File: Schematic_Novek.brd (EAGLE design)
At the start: 160 x 100 mm, 42 parts, among them IC1 STM32F10XCXT6, J2 1X2-3.5MM, J3 1X2-3.5MM, Q1 2N2907, U1 BQ21040, U2 MAX17048G+T10, U3 HX711

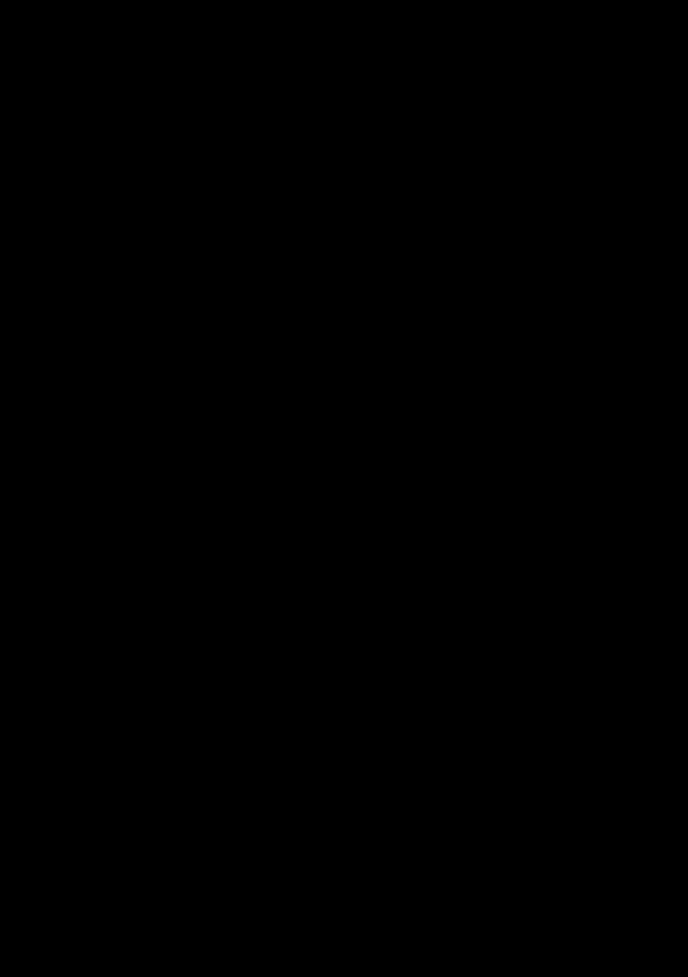
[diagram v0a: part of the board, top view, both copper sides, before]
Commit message: Adds sensor ports
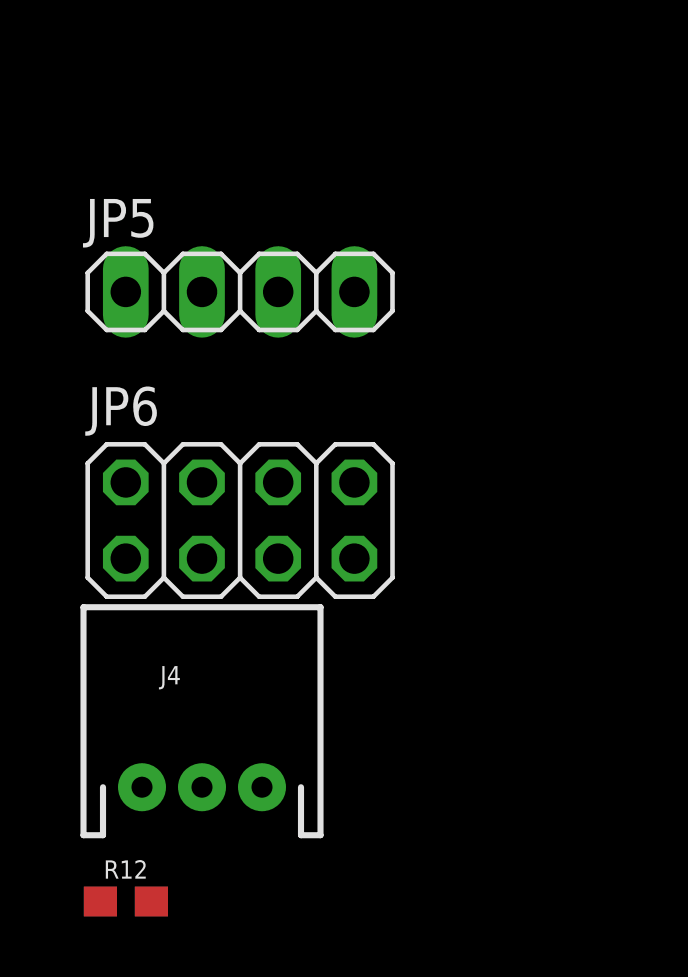
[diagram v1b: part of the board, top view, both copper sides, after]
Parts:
- added J4: (no value), SparkFun-Connectors:JST-3-PTH
- added JP5: (no value), pinhead:1X04
- added JP6: (no value), pinhead:2X04
- added R12: 10k, SparkFun-Resistors:0603
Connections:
- new net DATA_DHT: IC1.17, J4.2
- new net ESP8266_RX: IC1.12, JP6.2
- new net ESP8266_TX: IC1.13, JP6.7
- net 3.3V: now also C15.2, J4.1, JP5.3, JP6.1, Q1.E, R12.1, U3.1, U3.16
- net DOUT_HX: now also IC1.14
- net GND: now also J4.3, JP5.4, JP6.8
- net N$6: now also JP6.5, R12.2; no longer C15.2, Q1.E, U3.1, U3.16
- net SCK_HX: now also IC1.15
- net SCL: now also JP5.1
- net SDA: now also JP5.2
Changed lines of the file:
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@@
 <attribute name="NAME" x="-46.53" y="-203.28" size="1.27" layer="25" rot="R180"/>
+</element>
+<element name="JP5" library="pinhead" library_urn="urn:adsk.eagle:library:325" package="1X04" package3d_urn="urn:adsk.eagle:package:22407/2" value="" x="-46.99" y="-223.52" smashed="yes">
+<attribute name="NAME" x="-52.1462" y="-221.6912" size="1.27" layer="25" ratio="10"/>
+<attribute name="POPULARITY" value="91" x="-46.99" y="-223.52" size="1.778" layer="27" display="off"/>
+<attribute name="VALUE" x="-52.07" y="-226.695" size="1.27" layer="27"/>
+</element>
+<element name="JP6" library="pinhead" library_urn="urn:adsk.eagle:library:325" package="2X04" package3d_urn="urn:adsk.eagle:package:22461/2" value="" x="-46.99" y="-231.14" smashed="yes">
+<attribute name="NAME" x="-52.07" y="-227.965" size="1.27" layer="25" ratio="10"/>
+<attribute name="POPULARITY" value="47" x="-46.99" y="-231.14" size="1.778" layer="27" display="off"/>
+<attribute name="VALUE" x="-52.07" y="-235.585" size="1.27" layer="27"/>
+</element>
+<element name="J4" library="SparkFun-Connectors" package="JST-3-PTH" value="" x="-48.26" y="-240.03" smashed="yes">
+<attribute name="NAME" x="-49.657" y="-236.601" size="0.6096" layer="25" font="vector" ratio="20"/>
+<attribute name="PROD_ID" value="WIRE-10037" x="-48.26" y="-240.03" size="1.778" layer="27" display="off"/>
+<attribute name="SF_ID" value="PRT-09915" x="-48.26" y="-240.03" size="1.778" layer="27" display="off"/>
+<attribute name="VALUE" x="-49.911" y="-237.49" size="0.6096" layer="27" font="vector" ratio="20"/>
+</element>
+<element name="R12" library="SparkFun-Resistors" package="0603" value="10k" x="-50.8" y="-243.84" smashed="yes">
+<attribute name="NAME" x="-50.8" y="-243.078" size="0.6096" layer="25" font="vector" ratio="20" align="bottom-center"/>
+<attribute name="PROD_ID" value="RES-00824" x="-50.8" y="-243.84" size="1.778" layer="27" display="off"/>
+<attribute name="VALUE" x="-50.8" y="-244.602" size="0.6096" layer="27" font="vector" ratio="20" align="top-center"/>
 </element>
 </elements>
@@
 <contactref element="U3" pad="10"/>
 <contactref element="U3" pad="9"/>
+<contactref element="JP5" pad="4"/>
+<contactref element="J4" pad="3"/>
+<contactref element="JP6" pad="8"/>
 <wire x1="-36.41" y1="-207.01" x2="-34.71" y2="-210.82" width="0" layer="19" extent="1-1"/>
 <wire x1="-36.41" y1="-199.39" x2="-36.41" y2="-207.01" width="0" layer="19" extent="1-1"/>
 <wire x1="-34.71" y1="-187.96" x2="-36.41" y2="-199.39" width="0" layer="19" extent="1-1"/>
+<wire x1="-43.18" y1="-223.52" x2="-34.71" y2="-210.82" width="0" layer="19" extent="1-1"/>
+<wire x1="-43.18" y1="-229.87" x2="-43.18" y2="-223.52" width="0" layer="19" extent="1-1"/>
+<wire x1="-46.26" y1="-240.03" x2="-43.18" y2="-229.87" width="0" layer="19" extent="1-1"/>
 <wire x1="-20.955" y1="-180.6" x2="-34.71" y2="-187.96" width="0" layer="19" extent="1-1"/>
 <wire x1="-23.495" y1="-175" x2="-20.955" y2="-180.6" width="0" layer="19" extent="1-1"/>
@@
 <contactref element="VR1" pad="P$5"/>
 <contactref element="C11" pad="2"/>
+<contactref element="U3" pad="16"/>
+<contactref element="C15" pad="2"/>
+<contactref element="U3" pad="1"/>
+<contactref element="Q1" pad="E"/>
+<contactref element="JP5" pad="3"/>
+<contactref element="J4" pad="1"/>
+<contactref element="JP6" pad="1"/>
+<contactref element="R12" pad="1"/>
+<wire x1="-45.72" y1="-223.52" x2="-34.71" y2="-207.01" width="0" layer="19" extent="1-1"/>
+<wire x1="-50.8" y1="-232.41" x2="-45.72" y2="-223.52" width="0" layer="19" extent="1-1"/>
+<wire x1="-50.26" y1="-240.03" x2="-50.8" y2="-232.41" width="0" layer="19" extent="1-1"/>
+<wire x1="-51.65" y1="-243.84" x2="-50.26" y2="-240.03" width="0" layer="19" extent="1-1"/>
+<wire x1="-26.035" y1="-180.6" x2="-34.71" y2="-207.01" width="0" layer="19" extent="1-1"/>
+<wire x1="-26.035" y1="-175" x2="-26.035" y2="-180.6" width="0" layer="19" extent="1-1"/>
+<wire x1="-36.83" y1="-176.53" x2="-26.035" y2="-175" width="0" layer="19" extent="1-1"/>
+<wire x1="-25.82" y1="-128.27" x2="-26.035" y2="-175" width="0" layer="19" extent="1-1"/>
 <wire x1="-25.37" y1="-118.43" x2="-25.82" y2="-128.27" width="0" layer="19" extent="1-1"/>
 <wire x1="-22.44" y1="-109.22" x2="-25.37" y2="-118.43" width="0" layer="19" extent="1-1"/>
@@
 <contactref element="U2" pad="7"/>
 <contactref element="IC1" pad="43"/>
+<contactref element="JP5" pad="2"/>
+<wire x1="-48.26" y1="-223.52" x2="-24.415" y2="-133.1" width="0" layer="19" extent="1-1"/>
 <wire x1="1.85" y1="-6.6" x2="-24.415" y2="-133.1" width="0" layer="19" extent="1-1"/>
 </signal>
@@
 <contactref element="U2" pad="8"/>
 <contactref element="IC1" pad="42"/>
+<contactref element="JP5" pad="1"/>
+<wire x1="-50.8" y1="-223.52" x2="-24.415" y2="-132.6" width="0" layer="19" extent="1-1"/>
 <wire x1="1.85" y1="-6.1" x2="-24.415" y2="-132.6" width="0" layer="19" extent="1-1"/>
 </signal>
@@
 <signal name="EP">
 <contactref element="U2" pad="9"/>
-</signal>
-<signal name="N$6">
-<contactref element="U3" pad="16"/>
-<contactref element="C15" pad="2"/>
-<contactref element="U3" pad="1"/>
-<contactref element="Q1" pad="E"/>
-<wire x1="-26.035" y1="-180.6" x2="-34.71" y2="-207.01" width="0" layer="19" extent="1-1"/>
-<wire x1="-26.035" y1="-175" x2="-26.035" y2="-180.6" width="0" layer="19" extent="1-1"/>
-<wire x1="-36.83" y1="-176.53" x2="-26.035" y2="-175" width="0" layer="19" extent="1-1"/>
 </signal>
 <signal name="N$5">
@@
 <signal name="DOUT_HX">
 <contactref element="U3" pad="12"/>
+<contactref element="IC1" pad="14"/>
+<wire x1="10.85" y1="-8.6" x2="-20.955" y2="-175" width="0" layer="19" extent="1-1"/>
 </signal>
 <signal name="SCK_HX">
 <contactref element="U3" pad="11"/>
+<contactref element="IC1" pad="15"/>
+<wire x1="10.85" y1="-8.1" x2="-19.685" y2="-175" width="0" layer="19" extent="1-1"/>
+</signal>
+<signal name="DATA_DHT">
+<contactref element="J4" pad="2"/>
+<contactref element="IC1" pad="17"/>
+<wire x1="10.85" y1="-7.1" x2="-48.26" y2="-240.03" width="0" layer="19" extent="1-1"/>
+</signal>
+<signal name="ESP8266_RX">
+<contactref element="JP6" pad="2"/>
+<contactref element="IC1" pad="12"/>
+<wire x1="9.1" y1="-10.85" x2="-50.8" y2="-229.87" width="0" layer="19" extent="1-1"/>
+</signal>
+<signal name="N$6">
+<contactref element="JP6" pad="5"/>
+<contactref element="R12" pad="2"/>
+<wire x1="-45.72" y1="-232.41" x2="-49.95" y2="-243.84" width="0" layer="19" extent="1-1"/>
+</signal>
+<signal name="ESP8266_TX">
+<contactref element="JP6" pad="7"/>
+<contactref element="IC1" pad="13"/>
+<wire x1="10.85" y1="-9.1" x2="-43.18" y2="-232.41" width="0" layer="19" extent="1-1"/>
 </signal>
 </signals>

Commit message: Component placement on board
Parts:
- removed JP3: (no value), pinhead:1X04
- removed R1: (no value), resistor:0204/7
- added R13: 1M, SparkFun-Resistors:0603
- moved R12 308.9 mm to (49.4, 48.4), flipped to the bottom
- moved JP6 289.8 mm to (46.7, 43.1), turned to 180 degrees
- moved J4 276.7 mm to (7.50, 31.0), turned to 90 degrees
- moved J3 265.2 mm to (62.4, 32.1), flipped to the bottom, turned to 90 degrees
- moved J2 255.7 mm to (62.3, 25.2), flipped to the bottom, turned to 90 degrees
- moved C14 249.7 mm to (45.7, 32.9)
- moved R11 243.9 mm to (50.1, 32.8)
- moved JP5 243.8 mm to (7.20, 14.2)
- moved C13 243.2 mm to (50.0, 28.3), turned to 180 degrees
- moved C15 240.0 mm to (45.6, 18.9)
- moved R10 238.1 mm to (50.1, 30.4)
- moved C16 232.9 mm to (42.7, 8.50)
- moved R9 230.7 mm to (50.1, 26.3)
- moved R8 225.5 mm to (50.1, 24.5)
- moved U3 214.4 mm to (43.7, 26.4), turned to 90 degrees
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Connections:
- removed net 5V: JP3.3
- removed net FTDI_RX: IC1.30, JP3.1
- removed net FTDI_TX: IC1.31, JP3.2
- net GND: now also J1.SHIELD1, J1.SHIELD2, J1.SHIELD3, J2.1; no longer JP3.4
- net OSCIN: now also R13.2; no longer R1.2
- net OSCOUT: now also R13.1; no longer R1.1

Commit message: Started routing
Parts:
- moved C2 0.60 mm to (31.0, 30.4), flipped to the bottom
- moved C1 0.32 mm to (24.4, 30.4), flipped to the bottom
- moved R13 0.10 mm to (27.6, 31.4), flipped to the bottom, turned to 0 degrees
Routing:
- net 3.3V: track 0.00 -> 279.6 mm, vias 0 -> 1
- net VBATT: track 0.00 -> 97.2 mm, vias 0 -> 1
- net GND: track 0.00 -> 55.4 mm, vias 0 -> 1
- net SDA: track 0.00 -> 51.6 mm, vias 0 -> 1
- net SCL: track 0.00 -> 51.4 mm, vias 0 -> 1
- net INTRPT_MAX: track 0.00 -> 47.6 mm, vias 0 -> 1
- net CHG_STATUS: track 0.00 -> 43.8 mm, vias 0 -> 2
- net DATA_DHT: track 0.00 -> 36.2 mm, vias 0 -> 1
- net N$7: track 0.00 -> 34.4 mm
- net BOOT1: track 0.00 -> 31.3 mm, vias 0 -> 1
- net RESET: track 0.00 -> 29.5 mm
- net ESP8266_TX: track 0.00 -> 26.8 mm, vias 0 -> 1
- net ESP8266_RX: track 0.00 -> 26.0 mm, vias 0 -> 2
- net DOUT_HX: track 0.00 -> 23.8 mm
- net SCK_HX: track 0.00 -> 23.5 mm
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- added copper zone on layer 1, net GND
- added copper zone on layer 16, net GND
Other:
- board size 160 x 100 mm -> 66 x 66 mm

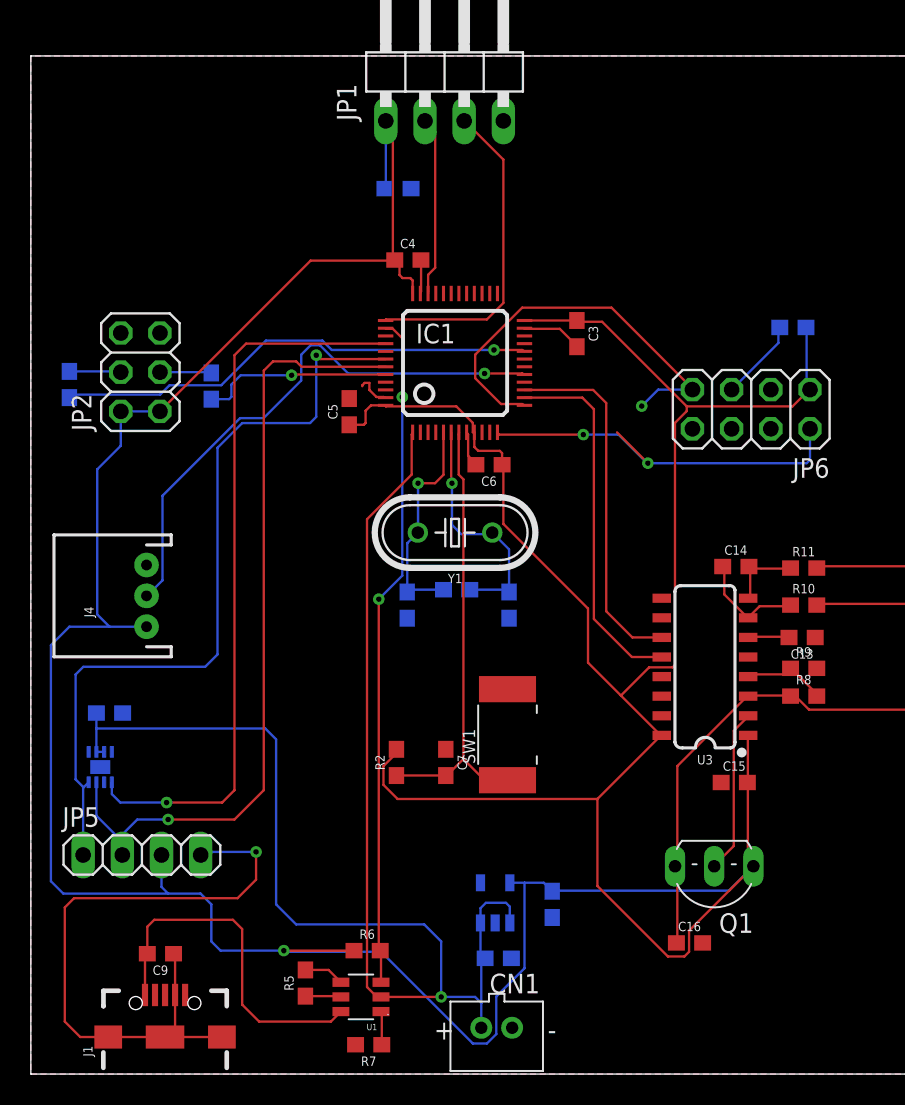
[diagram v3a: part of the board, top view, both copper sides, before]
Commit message: Routing of signals
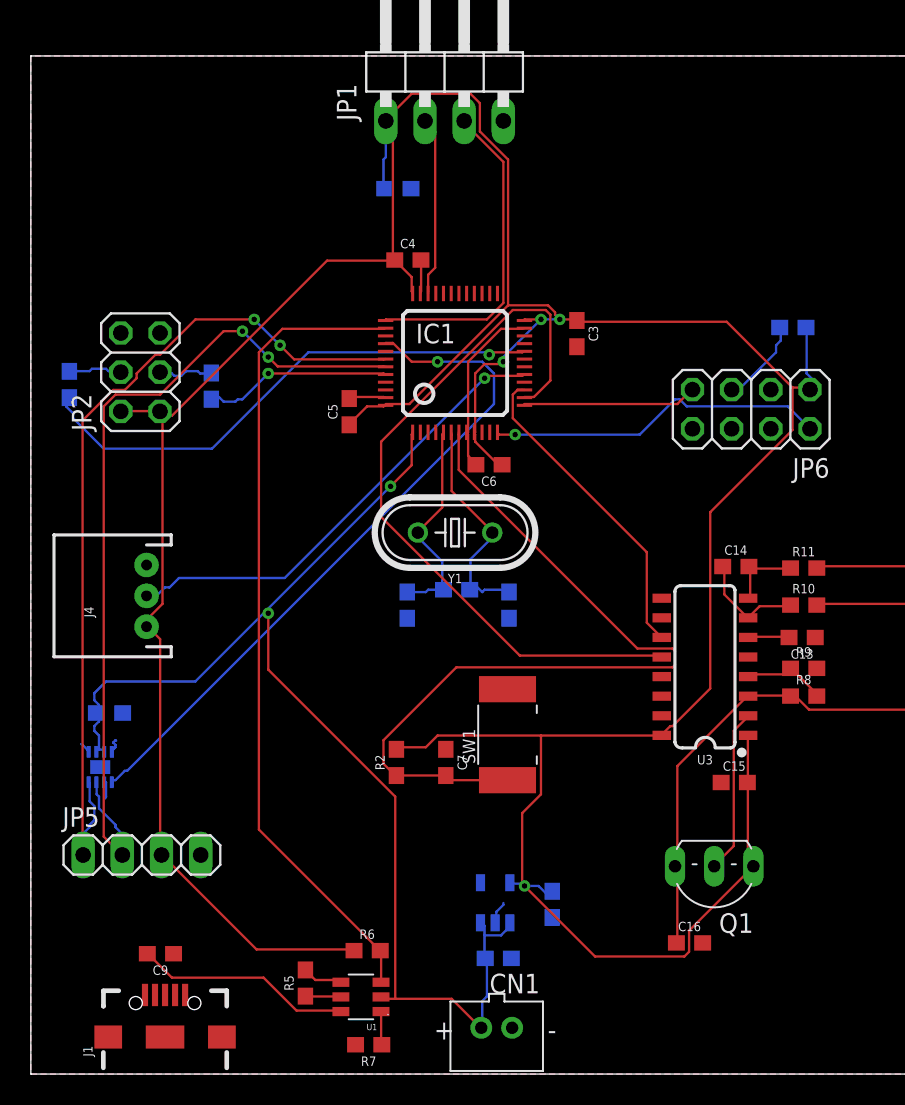
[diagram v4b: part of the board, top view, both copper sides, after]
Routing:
- net 3.3V: track 279.6 -> 244.9 mm, vias 1 -> 4
- net GND: track 55.4 -> 22.8 mm, vias 1 -> 0
- net DOUT_HX: track 23.8 -> 47.9 mm
- net RESET: track 29.5 -> 53.2 mm
- net VBATT: track 97.2 -> 79.1 mm, vias 1 -> 2
- net ESP8266_TX: track 26.8 -> 11.4 mm, vias 1 -> 0
- net CHG_STATUS: track 43.8 -> 53.0 mm, vias 2 -> 0
- net VBUS: track 23.1 -> 14.1 mm
- net DATA_DHT: track 36.2 -> 30.4 mm
- net SCL: track 51.4 -> 57.0 mm, vias 1 -> 2
- net SDA: track 51.6 -> 56.2 mm, vias 1 -> 2
- net ESP8266_RX: track 26.0 -> 22.1 mm, vias 2 -> 1
- net BOOT1: track 31.3 -> 34.4 mm
- net SCK_HX: track 23.5 -> 20.6 mm
- net INTRPT_MAX: track 47.6 -> 44.8 mm
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
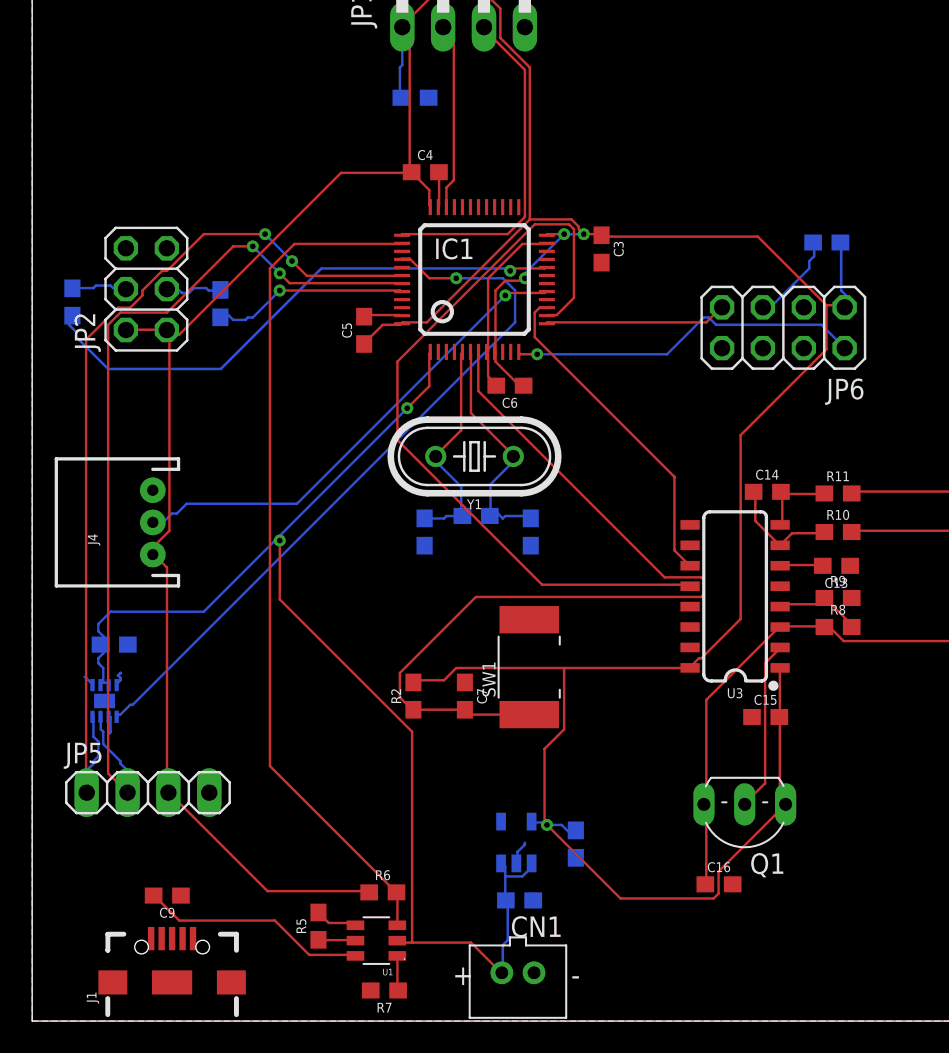
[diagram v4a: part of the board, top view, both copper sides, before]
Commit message: Completes routing
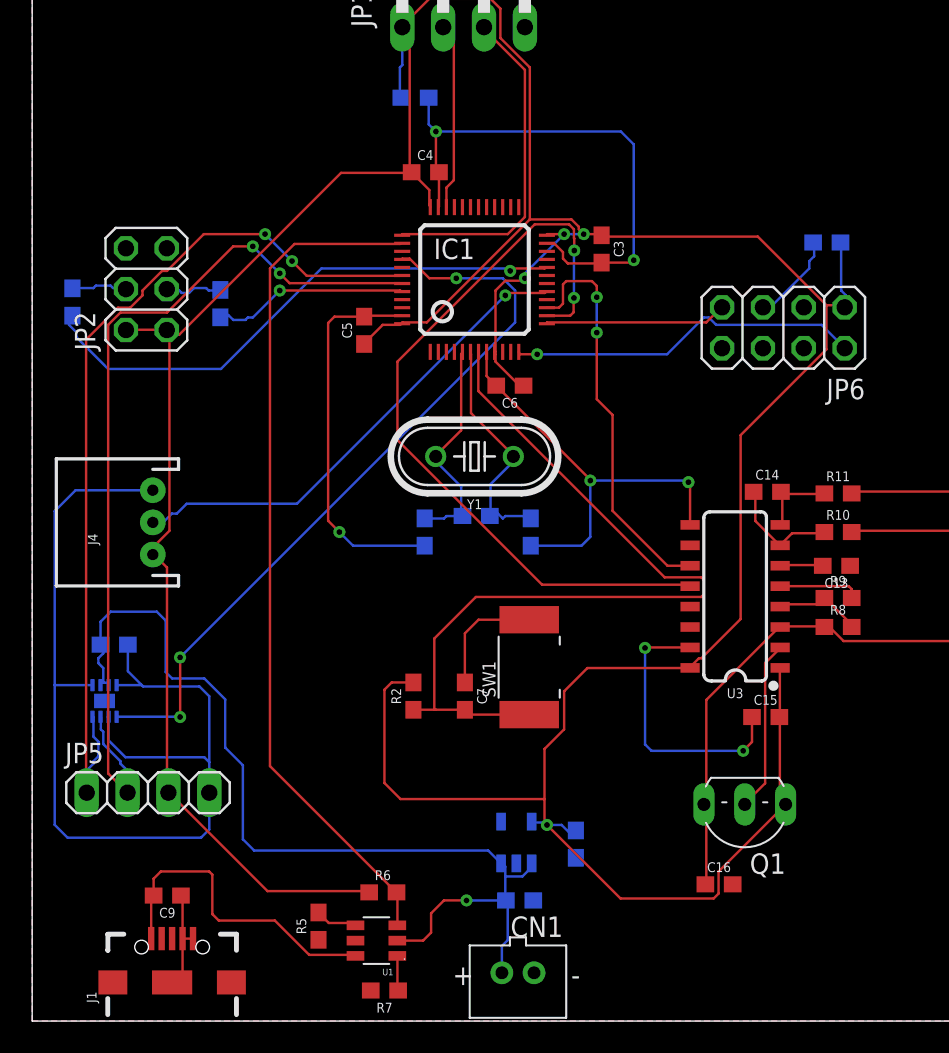
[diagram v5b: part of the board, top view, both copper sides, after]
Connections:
- removed net VBATT: C10.2, C12.1, CN1.1, IC1.1, U1.2, U2.2, U2.3, VR1.P$1, VR1.P$3
- new net BATT: C10.2, C12.1, CN1.1, U1.2, U2.2, U2.3, VR1.P$1, VR1.P$3
- new net VBHT: IC1.1
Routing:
- net GND: track 22.8 -> 184.2 mm, vias 0 -> 7
- net VBATT: track 79.1 -> 0.00 mm, vias 2 -> 0
- net BATT: track 0.00 -> 60.6 mm, vias 0 -> 1
- net 3.3V: track 244.9 -> 252.4 mm
- net VBUS: track 14.1 -> 20.1 mm
- net SCK_HX: track 20.6 -> 25.2 mm, vias 0 -> 2
- net INTRPT_MAX: track 44.8 -> 47.0 mm, vias 1 -> 3
- net RESET: track 53.2 -> 51.9 mm
- net DOUT_HX: track 47.9 -> 48.4 mm, vias 0 -> 2
